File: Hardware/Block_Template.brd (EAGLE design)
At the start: 30.5 x 44.5 mm, 11 parts, among them U2 EDISON_CONNECTOR_FULLMOUNTING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, U3 EDISON_CONNECTOR_FULLHEADER

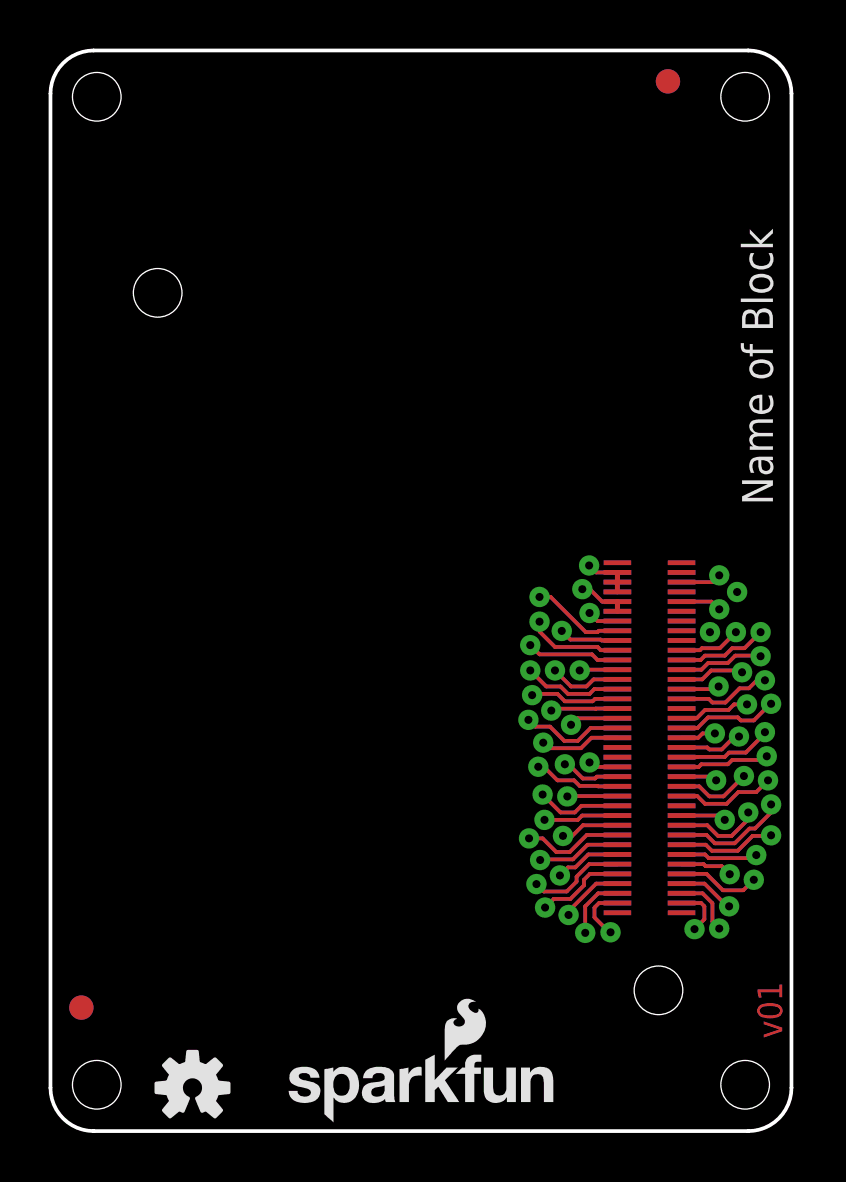
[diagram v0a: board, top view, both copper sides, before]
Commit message: updated footprints to remove jumpers between connector pins. Renamed Connectors to J1 and J2. Locked vias, holes, connectors, and logos.  Trying to keep things standard for future builds
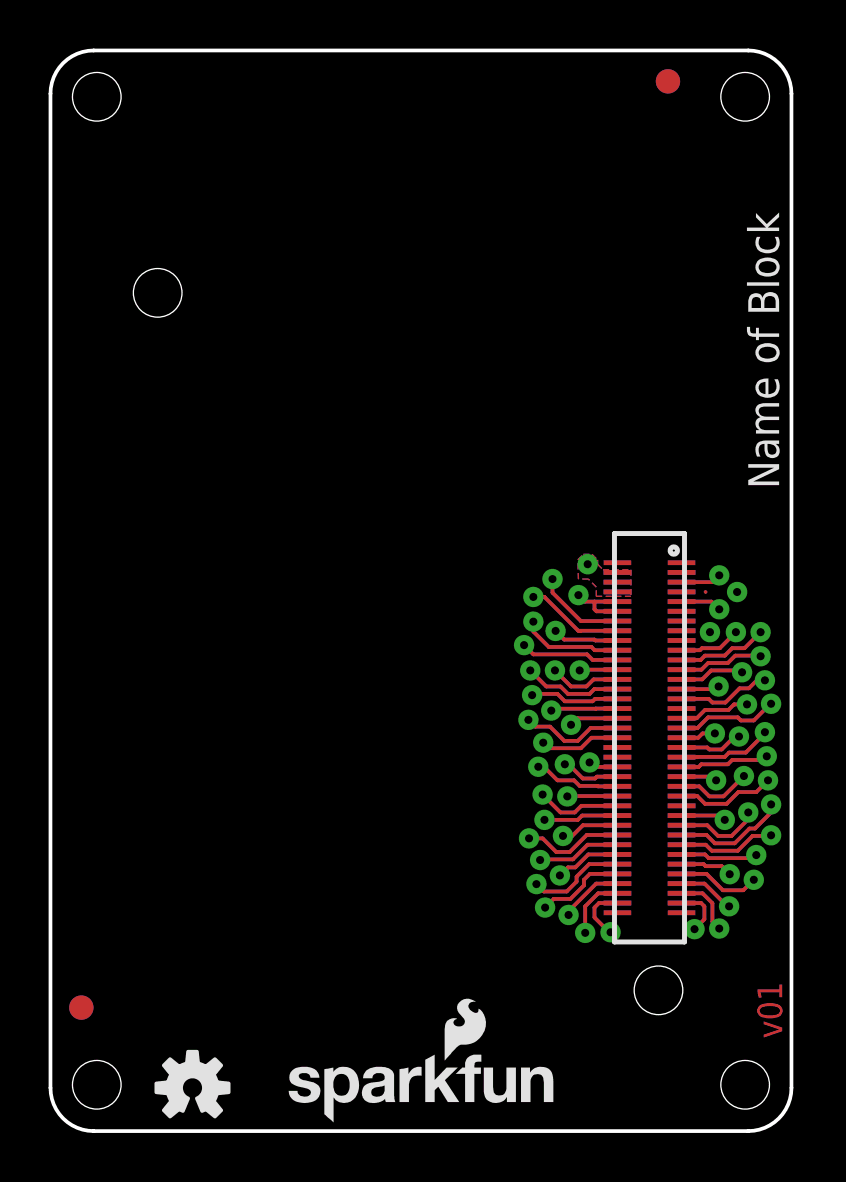
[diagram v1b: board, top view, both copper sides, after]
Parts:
- renumbered U2 to J1, U3 to J2
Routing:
- net 1.8V: track 2.57 -> 7.43 mm
- net VSYS: track 4.56 -> 0.00 mm
- net 3.3V: track 4.51 -> 6.02 mm
- net USB_VBUS: track 7.67 -> 8.18 mm
- net USB_DN: track 7.86 -> 8.36 mm
- net USB_DP: track 4.90 -> 5.41 mm
- added copper zone on layer 1, net VSYS
- added copper zone on layer 16, net VSYS
